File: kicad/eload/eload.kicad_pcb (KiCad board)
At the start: 2 copper layers, 67 parts, among them J201 Conn_01x15_Male, J202 Conn_01x15_Male, J301 USB_B_Micro, J501 LOAD, Q301 MMBT3904, Q302 MMBT3904, Q501 FDP6030BL, SW201 RESET_BTN, SW202 FLASH_BTN, U201 ESP-12F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

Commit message: Version 0.2
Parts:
- added H401: MountingHole, Mounting_Holes:MountingHole_2.5mm_Pad_Via, F.Cu at (68.1, 147.8)
- added H402: MountingHole, Mounting_Holes:MountingHole_2.5mm_Pad_Via, F.Cu at (170.8, 147.3)
- added H403: MountingHole, Mounting_Holes:MountingHole_2.5mm_Pad_Via, F.Cu at (67.6, 85.9)
- added H404: MountingHole, Mounting_Holes:MountingHole_2.5mm_Pad_Via, F.Cu at (170.7, 85.3)
- added HS501: Heatsink, Heatsinks:Heatsink_Fischer_SK104-STCB_35x13mm__2xDrill3.5mm_ScrewM3, F.Cu at (68.6, 124.5)
- moved J501 89.3 mm to (69.8, 101.6), turned to 90 degrees
- moved C408 70.6 mm to (86.6, 95.1)
- moved U402 70.1 mm to (82.0, 95.2)
- moved C407 69.7 mm to (77.5, 95.1)
- moved SW201 65.2 mm to (100.3, 91.4), turned to 180 degrees
- moved SW202 65.0 mm to (100.3, 97.8), turned to 180 degrees
- moved J201 61.9 mm to (112.8, 109.2)
- moved J202 45.5 mm to (111.8, 83.8)
- moved R201 45.2 mm to (113.5, 91.4), turned to 180 degrees
- moved R202 45.2 mm to (113.5, 96.8), turned to 180 degrees
- moved D201 44.6 mm to (113.5, 94.2), turned to 180 degrees
- moved R209 43.9 mm to (113.5, 105.9), turned to 180 degrees
- moved R203 42.7 mm to (113.5, 99.1), turned to 180 degrees
- moved R204 33.9 mm to (104.4, 85.0), turned to 180 degrees
- moved R205 33.8 mm to (104.4, 82.8), turned to 180 degrees
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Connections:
- J202 pad 12: /ESP8266-E12/GPIO3 -> /ESP8266-E12/ESP_RXD0
- J202 pad 13: /ESP8266-E12/GPIO1 -> /ESP8266-E12/ESP_TXD0
- Q501 pad 1: Net-(J501-Pad1) -> Net-(Q501-Pad1)
- Q501 pad 2: Net-(Q501-Pad2) -> Net-(J501-Pad1)
- R503 pad 2: /OPAMPS and MOSFET/DAC_IN -> GND
- U201 pad 15: /ESP8266-E12/GPIO3 -> /ESP8266-E12/ESP_RXD0
- U201 pad 16: /ESP8266-E12/GPIO1 -> /ESP8266-E12/ESP_TXD0
- U501 pad 2: GND -> Net-(R503-Pad1)
- U501 pad 3: Net-(R503-Pad1) -> /OPAMPS and MOSFET/DAC_IN
- U501 pad 8: Net-(Q501-Pad2) -> Net-(Q501-Pad1)
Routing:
- net +5V: track 0.00 -> 199.6 mm, vias 0 -> 1
- net +3V3: track 0.00 -> 138.4 mm, vias 0 -> 3
- net /USB to UART/ESP_RESET: track 0.00 -> 100.9 mm, vias 0 -> 1
- net /ESP8266-E12/ESP_GPIO0: track 0.00 -> 98.0 mm, vias 0 -> 4
- net Net-(Q501-Pad3): track 0.00 -> 84.5 mm
- net GND: track 0.00 -> 84.3 mm, vias 0 -> 280
- net /ESP8266-E12/ESP_TXD0: track 0.00 -> 79.1 mm
- net /ESP8266-E12/ESP_RXD0: track 0.00 -> 77.7 mm, vias 0 -> 2
- net /OPAMPS and MOSFET/ADC_OUT: track 0.00 -> 77.0 mm, vias 0 -> 2
- net /external DAC/DAC_SPI_CS: track 0.00 -> 58.0 mm
- net /external DAC/DAC_SPI_DI: track 0.00 -> 53.3 mm
- net /ESP8266-E12/CH_PD: track 0.00 -> 50.9 mm, vias 0 -> 1
- net /external DAC/DAC_SPI_CLK: track 0.00 -> 44.7 mm
- net /ESP8266-E12/GPIO2: track 0.00 -> 37.0 mm, vias 0 -> 1
- net /ESP8266-E12/GPIO16: track 0.00 -> 31.7 mm, vias 0 -> 1
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- added copper zone on B.Cu, net GND
- added copper zone on F.Cu, net GND
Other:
- board outline added: 115 x 73 mm
- board text added: "+"
- board text added: "-"
- board text added: "0"
- board text added: "1"
- board text added: "2"
- board text added: "3"
- board text added: "3.3"
- board text added: "4"
- board text added: "5"
- board text added: "5V"
- board text added: "6"
- board text added: "7"
- board text added: "8"
- board text added: "A0"
- board text added: "EN"
- board text added: "ESP8266 Electronic Load v0.2 dimtass - 2018 www.stupid-projects.com"
- board text added: "G"
- board text added: "LOAD+"
- board text added: "LOAD-"
- board text added: "R"
- board text added: "RST"
- board text added: "S1"
- board text added: "S2"
- board text added: "S3"
- board text added: "SC"
- board text added: "SK"
- board text added: "SO"
- board text added: "T"

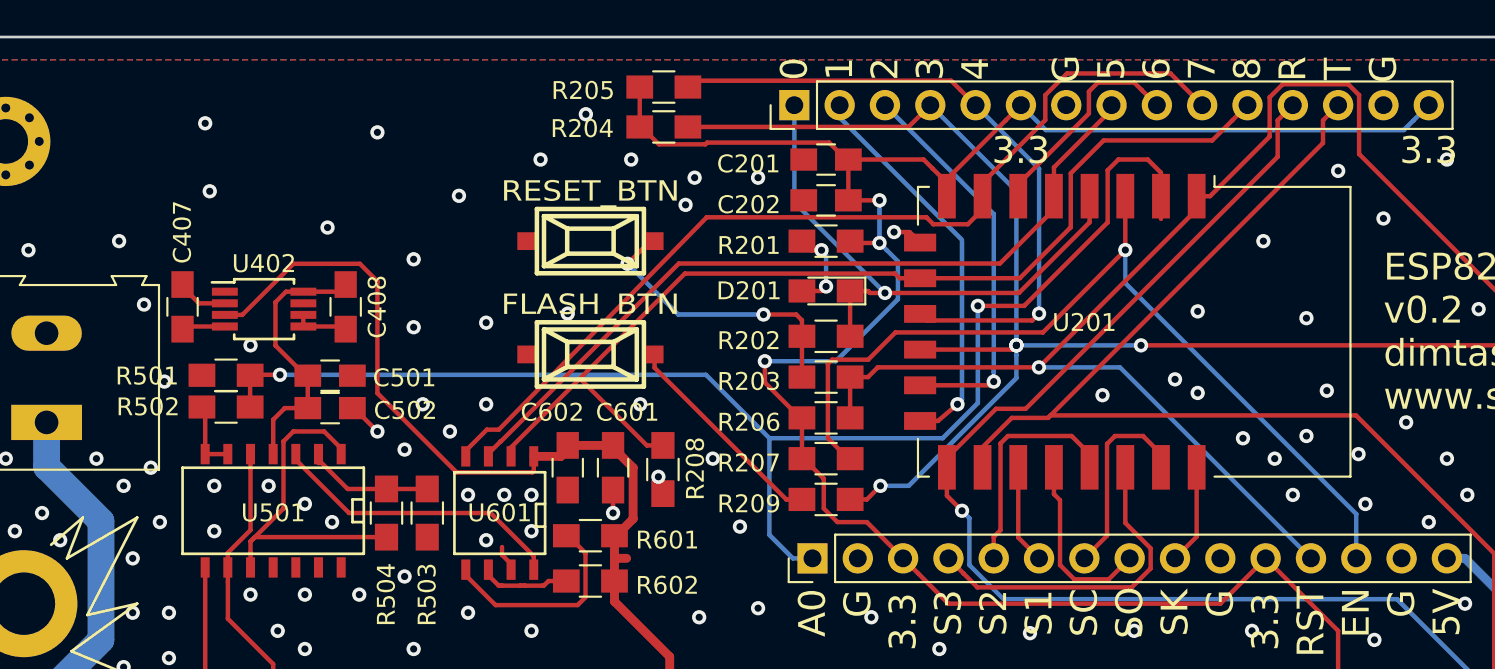
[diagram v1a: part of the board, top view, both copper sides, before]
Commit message: Added an RC filter in the ADC input
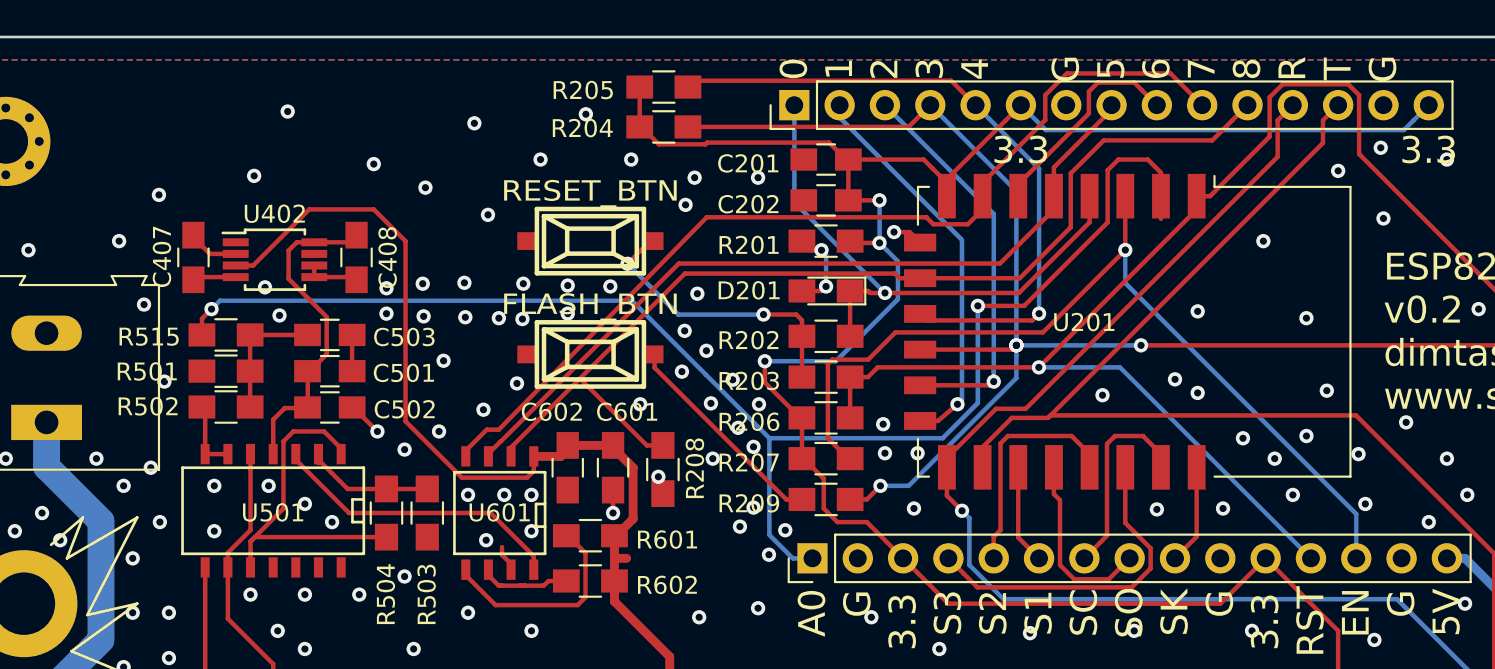
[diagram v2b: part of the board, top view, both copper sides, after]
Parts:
- added C503: 10uF, Capacitors_SMD:C_0805_HandSoldering, F.Cu at (85.7, 96.7)
- added R515: 15K, Resistors_SMD:R_0805_HandSoldering, F.Cu at (79.9, 96.7)
- R501: value 100K -> 1K
- R502: value 1M -> 10K
- moved C407 2.83 mm to (78.1, 92.4)
- moved C408 2.83 mm to (87.2, 92.4)
- moved U402 2.83 mm to (82.7, 92.5)
- moved C501 0.25 mm to (85.7, 98.7)
- moved R501 0.23 mm to (79.9, 98.7)
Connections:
- R501 pad 2: /OPAMPS and MOSFET/ADC_OUT -> Net-(C503-Pad1)
- R502 pad 2: /OPAMPS and MOSFET/ADC_OUT -> Net-(C503-Pad1)
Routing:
- net Net-(C503-Pad1): track 0.00 -> 7.06 mm
- net /OPAMPS and MOSFET/ADC_OUT: track 77.0 -> 80.9 mm
- net +5V: track 199.6 -> 202.8 mm
- net +10V: track 15.2 -> 18.4 mm
- net GND: track 84.3 -> 86.3 mm, vias 280 -> 310
- net (no net): vias 0 -> 1

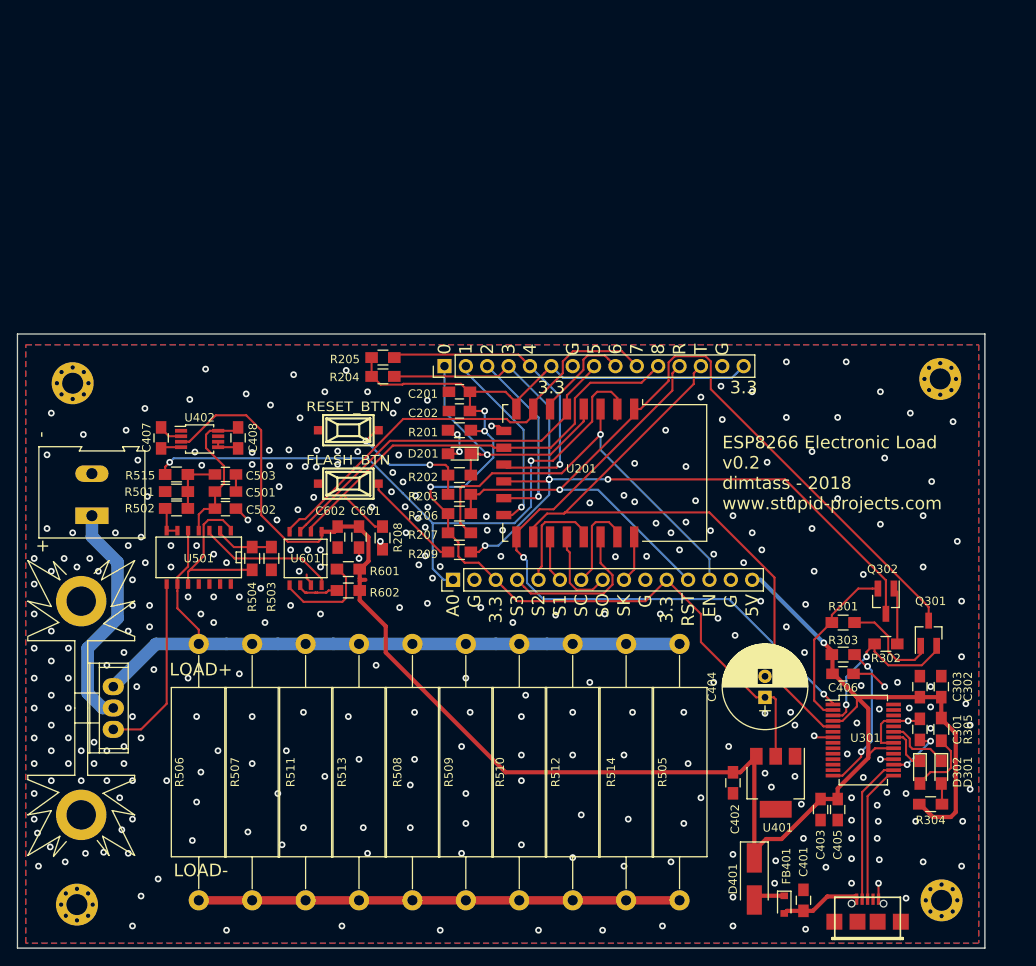
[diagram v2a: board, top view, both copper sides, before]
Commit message: Moved block terminal on top
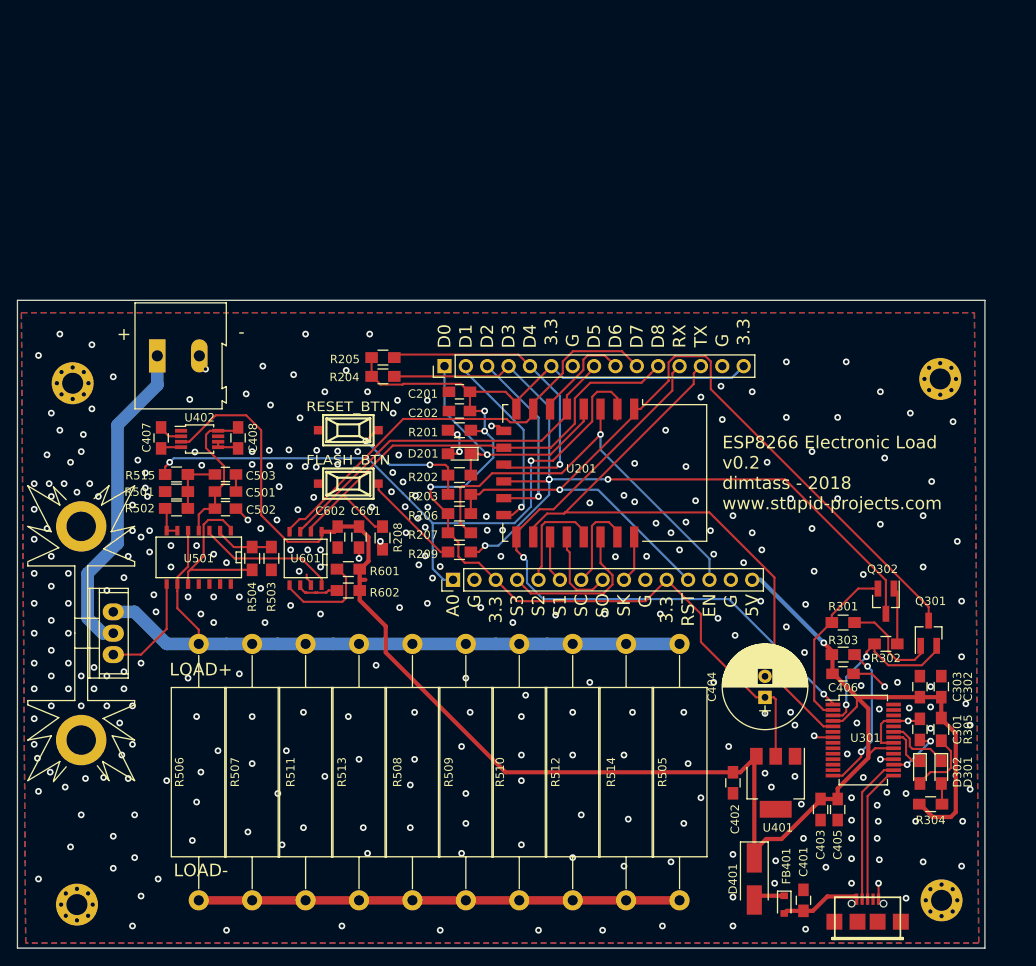
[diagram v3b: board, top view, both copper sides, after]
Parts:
- moved J501 20.5 mm to (77.6, 82.6), turned to 0 degrees
- moved HS501 8.89 mm to (68.6, 115.6)
- moved Q501 8.89 mm to (72.4, 115.6)
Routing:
- net Net-(J501-Pad1): track 27.6 -> 38.4 mm
- net Net-(Q501-Pad1): track 21.8 -> 12.9 mm
- net Net-(Q501-Pad3): track 84.5 -> 83.9 mm
- net GND: vias 310 -> 324
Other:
- board size 115 x 73 mm -> 115 x 77 mm
- board text added: "D0"
- board text added: "D1"
- board text added: "D2"
- board text added: "D3"
- board text added: "D4"
- board text added: "D5"
- board text added: "D6"
- board text added: "D7"
- board text added: "D8"
- board text added: "RX"
- board text added: "TX"
- board text removed: "0"
- board text removed: "1"
- board text removed: "2"
- board text removed: "3"
- board text removed: "4"
- board text removed: "5"
- board text removed: "6"
- board text removed: "7"
- board text removed: "8"
- board text removed: "R"
- board text removed: "T"
